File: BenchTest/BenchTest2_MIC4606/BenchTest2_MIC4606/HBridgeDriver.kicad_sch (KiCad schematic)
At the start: 26 parts, among them Q5 Q_NMOS_DGS, Q6 Q_NMOS_DGS, Q7 Q_PMOS_DGS, Q8 Q_PMOS_DGS

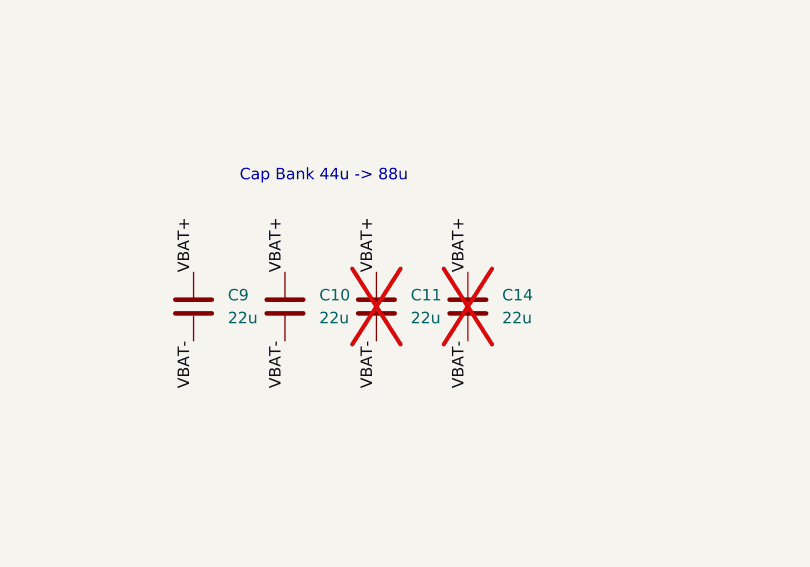
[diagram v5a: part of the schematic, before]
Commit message: Footprint / Capacitor Assignment
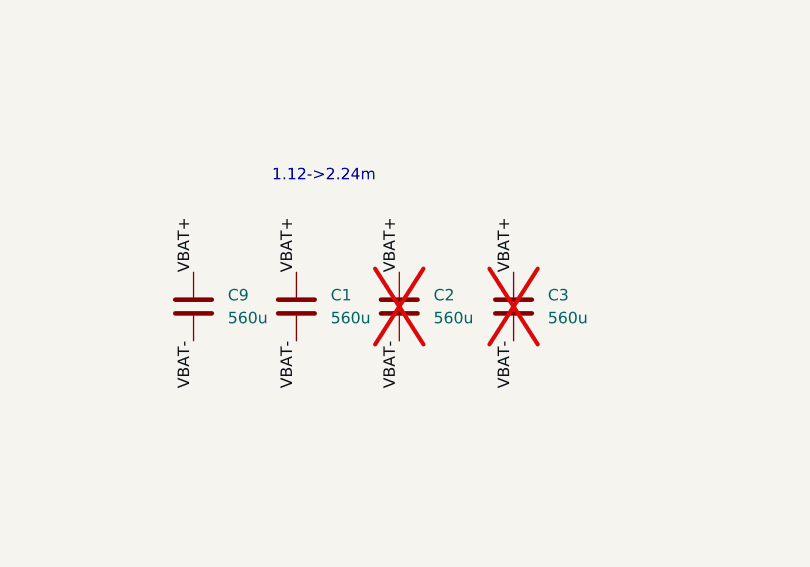
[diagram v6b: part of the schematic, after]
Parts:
- removed C10, C11, C14: 22u, symbol Device:C
- added C1, C2, C3: 560u, Capacitor_THT:C_Radial_D18.0mm_H35.5mm_P7.50mm, symbol Device:C
- C9: value 22u -> 560u; footprint (none) -> Capacitor_THT:C_Radial_D18.0mm_H35.5mm_P7.50mm; P/N 226AVG100MFBJ -> EPAG201ELL561MM45S
- D10, D11, D7, D8, D9: footprint (none) -> Diode_SMD:D_0603_1608Metric_Pad1.05x0.95mm_HandSolder
- R17: footprint (none) -> Resistor_SMD:R_0402_1005Metric_Pad0.72x0.64mm_HandSolder
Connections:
- net VBAT+: now also C1.1, C2.1, C3.1
- net VBAT-: now also C1.2, C2.2, C3.2
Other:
- note added: "1.12->2.24m"
- note removed: "Cap Bank 44u -> 88u"
